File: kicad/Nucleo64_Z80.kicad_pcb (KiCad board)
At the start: 2 copper layers, 68.6 x 57.2 mm, 28 parts, among them J1 Conn_01x20_Pin, J2 Conn_01x20_Pin, J3 Qwiic_connector, J4 SD Card slot, J5 SD Card slot, U2 AS6C4008-55PCN, U3 Z80CPU, U4 74LS125

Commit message: Add Nucleo64_Z80 PCB revision 1.0
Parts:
- removed R5: 10K, Resistor_SMD:R_0805_2012Metric_Pad1.20x1.40mm_HandSolder
- added JP4: SolderJumper_2_Open, Jumper:SolderJumper-2_P1.3mm_Open_RoundedPad1.0x1.5mm, B.Cu at (158.4, 127.0)
- added JP5: SolderJumper_2_Bridged, Jumper:SolderJumper-2_P1.3mm_Bridged_RoundedPad1.0x1.5mm, B.Cu at (128.9, 99.2)
- added JP6: SolderJumper_2_Bridged, Jumper:SolderJumper-2_P1.3mm_Bridged_RoundedPad1.0x1.5mm, B.Cu at (128.9, 101.6)
- C1, C2: value C_Small -> 0.1uF
- JP1, JP2: value SolderJumper_2_Open -> SolderJumper_3_Bridged12; footprint Jumper:SolderJumper-2_P1.3mm_Open_RoundedPad1.0x1.5mm -> Jumper:SolderJumper-3_P1.3mm_Bridged12_RoundedPad1.0x1.5mm_NumberLabels
- R1: value R_Small -> 200
- REF**: moved to B.Cu
- moved REF** 55.0 mm to (128.4, 109.6), turned to -90 degrees
- moved JP3 44.3 mm to (158.4, 129.5)
- moved JP2 37.9 mm to (150.2, 132.9)
- moved JP1 37.2 mm to (126.4, 136.2)
- moved D4 2.54 mm to (115.6, 119.4)
- moved D3 2.54 mm to (115.6, 111.8)
- moved D5 2.54 mm to (115.6, 127.0)
- moved J3 2.54 mm to (116.8, 144.8)
- moved R6 2.54 mm to (113.0, 132.1)
- moved R7 2.54 mm to (113.0, 134.6)
- moved R8 2.54 mm to (113.0, 137.2)
- moved U1 2.54 mm to (139.7, 108.6)
- moved J4 1.27 mm to (123.8, 144.8)
- moved J5 1.27 mm to (136.5, 141.0)
- moved C1 1.27 mm to (141.0, 99.1)
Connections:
- JP1 pad 1: BANK_SEL0 -> PA4
- JP1 pad 2: A16 -> ~{SPI1_SS}
- JP2 pad 1: BANK_SEL1 -> VCC
- JP2 pad 2: A17 -> ~{INT}
- JP3 pad 1: BANK_SEL2 -> PC13
- JP3 pad 2: A18 -> ~{M1}
- U1 pad CN10_11: ~{INT} -> SPI1_SCLK
- U1 pad CN10_21: ~{RFSH} -> A14
- U1 pad CN10_23: BANK_SEL2 -> A13
- U1 pad CN10_31: SPI1_SCLK -> PB3
- U1 pad CN10_33: ~{WAIT} -> A15
- U1 pad CN7_23: A13 -> PC13
- U1 pad CN7_25: A14 -> PC14
- U1 pad CN7_27: A15 -> PC15
- U1 pad CN7_30: ~{M1} -> ~{WAIT}
- U1 pad CN7_32: ~{SPI1_SS} -> PA4
- U2 pad 1: A18 -> GND
- U4 pad 10: Net-(D1-A) -> GND
- U4 pad 8: A18 -> unconnected-(U4-Pad8)
- U4 pad 9: BANK_SEL2 -> GND
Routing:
- net BANK_SEL2: track 99.8 -> 0.00 mm, vias 5 -> 0
- net PC15: track 0.00 -> 57.2 mm, vias 0 -> 1
- net PC13: track 0.00 -> 53.3 mm, vias 0 -> 1
- net PC14: track 0.00 -> 44.0 mm, vias 0 -> 1
- net PB3: track 0.00 -> 43.7 mm, vias 0 -> 1
- net A18: track 42.0 -> 0.00 mm
- net ~{INT}: track 49.1 -> 7.62 mm, vias 2 -> 0
- net ~{WR}: track 111.4 -> 79.0 mm, vias 3 -> 2
- net ~{WAIT}: track 30.4 -> 56.7 mm, vias 0 -> 1
- net SPI1_SCLK: track 53.9 -> 79.4 mm, vias 2 -> 4
- net 3V3: track 47.3 -> 30.4 mm, vias 2 -> 1
- net PA4: track 0.00 -> 16.4 mm, vias 0 -> 1
- net VCC: track 173.8 -> 189.7 mm, vias 7 -> 10
- net ~{M1}: track 75.6 -> 60.7 mm, vias 3 -> 4
- net A10: track 104.1 -> 93.6 mm, vias 2 -> 4
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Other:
- board size 68.6 x 57.2 mm -> 68.6 x 53.3 mm
- board text added: "35"
- board text added: "Rev 1.0 Apr 29, 2024 @hanyazou"
- board text added: "https://github.com/hanyazou/Nucleo64_Z80"
- board text removed: "Rev 0.9 Mar 14, 2024 @hanyazou"

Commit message: Add Nucleo64_Z80 PCB revision 1.1
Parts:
- removed REF**: OSHW-Logo2_7.3x6mm_SilkScreen, Symbol:OSHW-Logo2_7.3x6mm_SilkScreen
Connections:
- J4 pad 5: VCC -> 3V3
- J5 pad 5: VCC -> 3V3
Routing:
- net 3V3: track 30.4 -> 52.1 mm, vias 1 -> 2
- net VCC: track 189.7 -> 172.8 mm, vias 10 -> 9
- net ~{SPI1_SS}: track 57.0 -> 58.3 mm
- net GND: track 229.0 -> 229.9 mm, vias 83 -> 82
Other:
- board text added: "Rev 1.1 May 18, 2024 @hanyazou"
- board text removed: "Rev 1.0 Apr 29, 2024 @hanyazou"

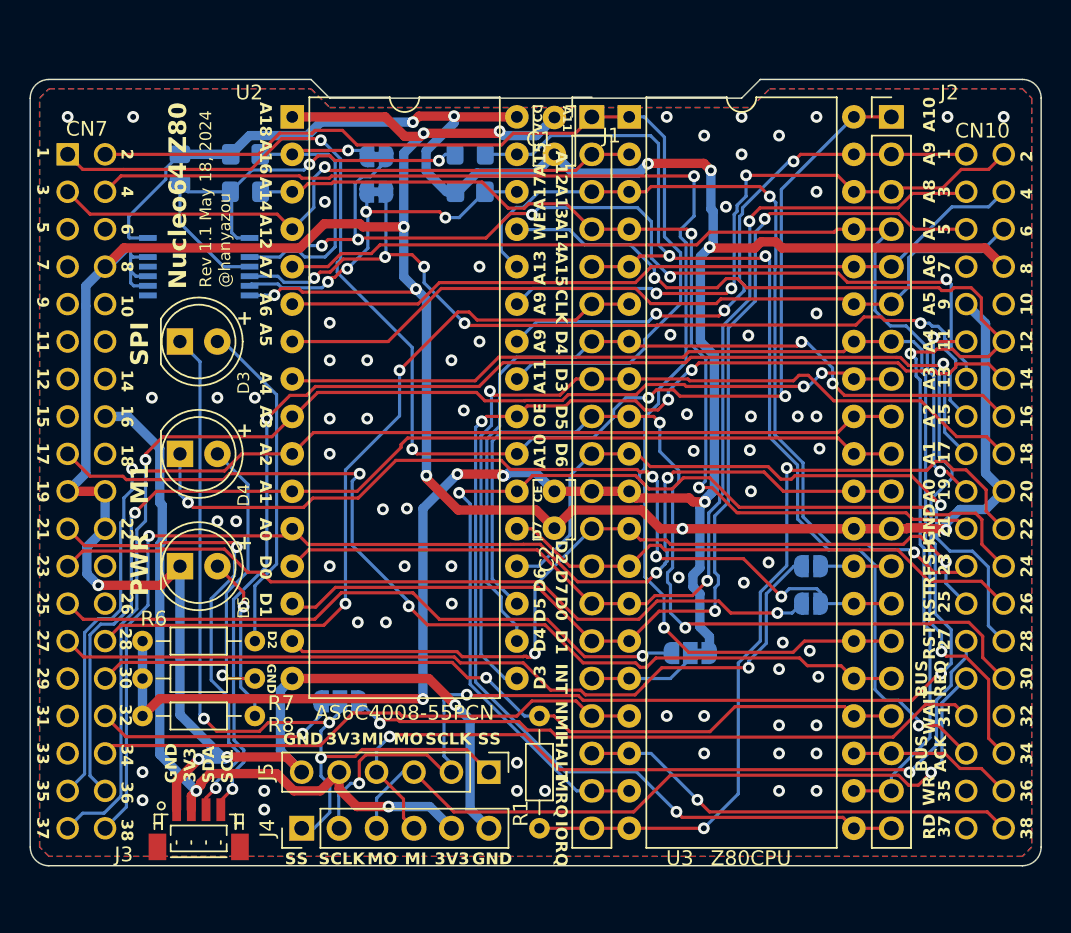
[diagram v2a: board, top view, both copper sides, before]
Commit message: Add Nucleo64_Z80 PCB revision 1.2
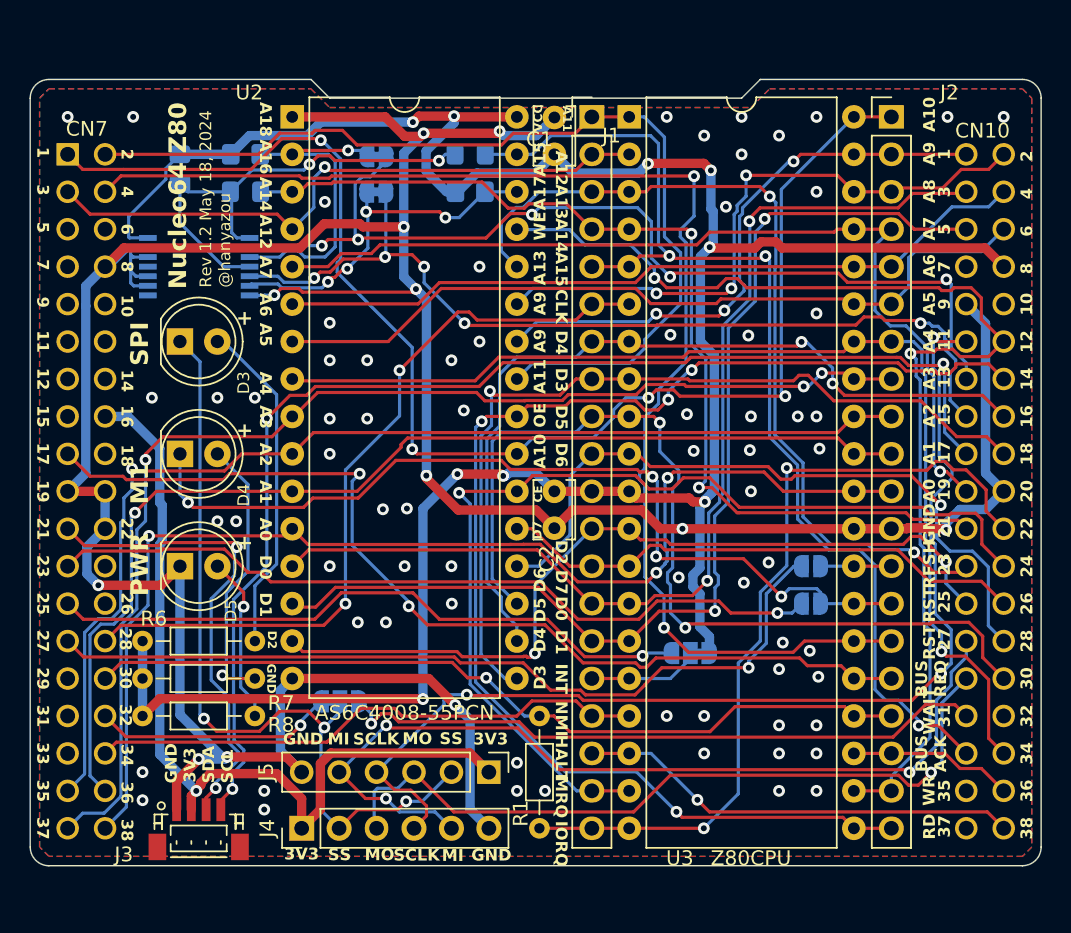
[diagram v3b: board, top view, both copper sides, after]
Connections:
- J4 pad 1: ~{SPI1_SS} -> 3V3
- J4 pad 2: SPI1_SCLK -> ~{SPI1_SS}
- J4 pad 4: SPI1_MISO -> SPI1_SCLK
- J4 pad 5: 3V3 -> SPI1_MISO
- J5 pad 1: ~{SPI1_SS} -> 3V3
- J5 pad 2: SPI1_SCLK -> ~{SPI1_SS}
- J5 pad 4: SPI1_MISO -> SPI1_SCLK
- J5 pad 5: 3V3 -> SPI1_MISO
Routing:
- net SPI1_MISO: track 54.5 -> 61.6 mm, vias 2 -> 3
- net 3V3: track 52.1 -> 58.1 mm, vias 2 -> 1
- net SPI1_SCLK: track 79.4 -> 74.9 mm, vias 4 -> 3
- net ~{SPI1_SS}: track 58.3 -> 55.2 mm
- net PB3: track 43.7 -> 44.4 mm
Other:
- board text added: "Rev 1.2 May 18, 2024 @hanyazou"
- board text removed: "Rev 1.1 May 18, 2024 @hanyazou"
